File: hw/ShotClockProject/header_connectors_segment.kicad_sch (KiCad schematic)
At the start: 4 parts, among them J1 Conn_01x06_Pin

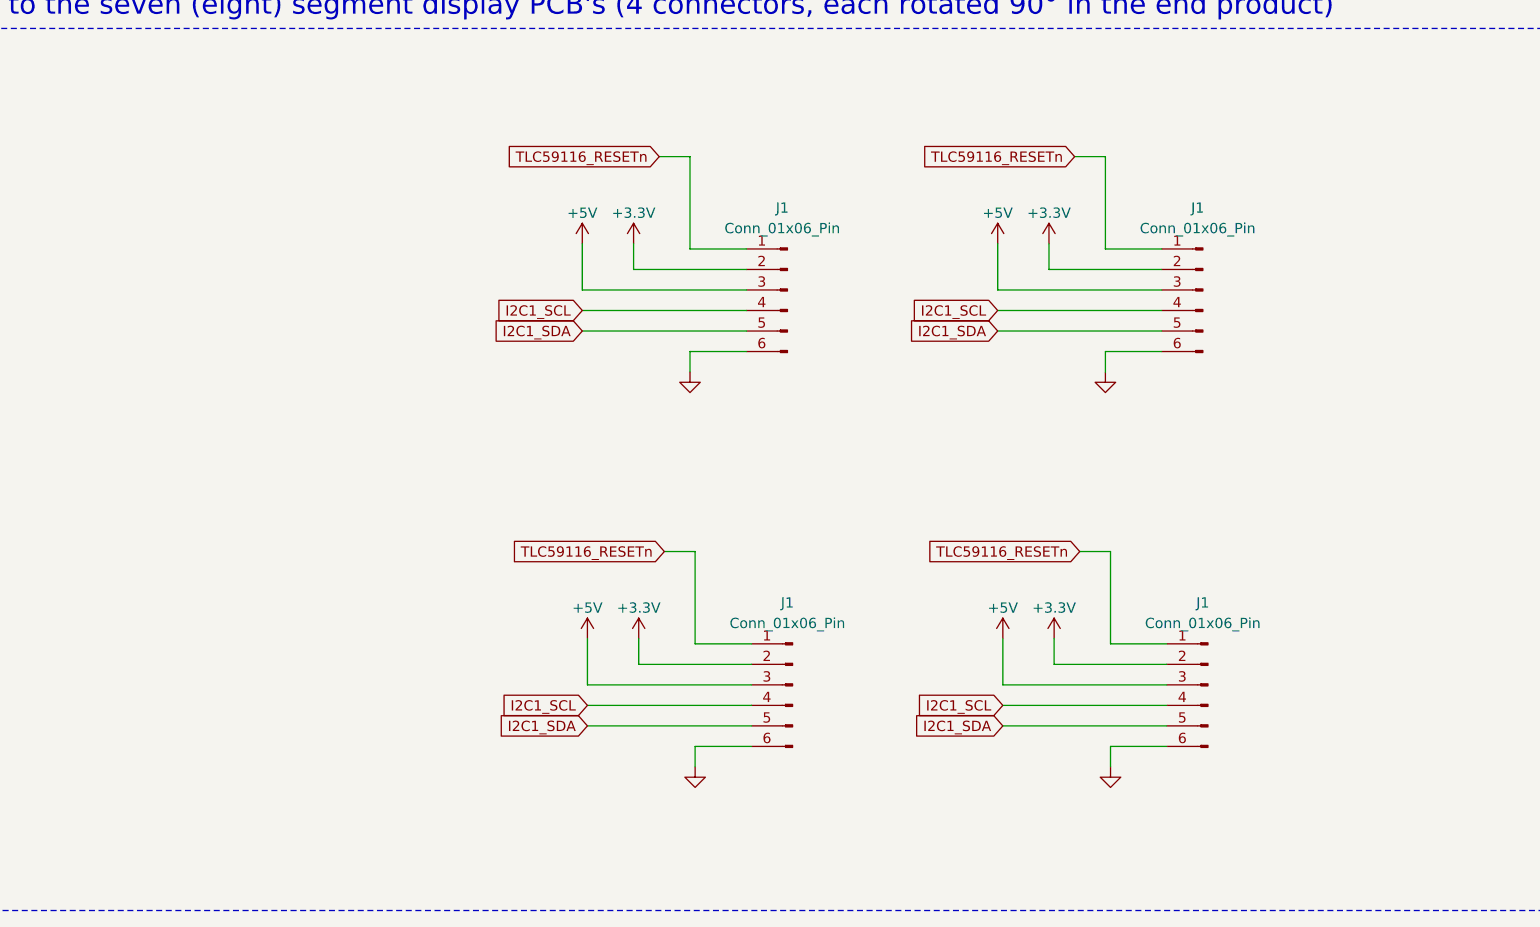
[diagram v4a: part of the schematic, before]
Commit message: Changed display connectors to JST PH 2.0mm
In docs, schematic and footprints
Both sides, connect with male/male cable
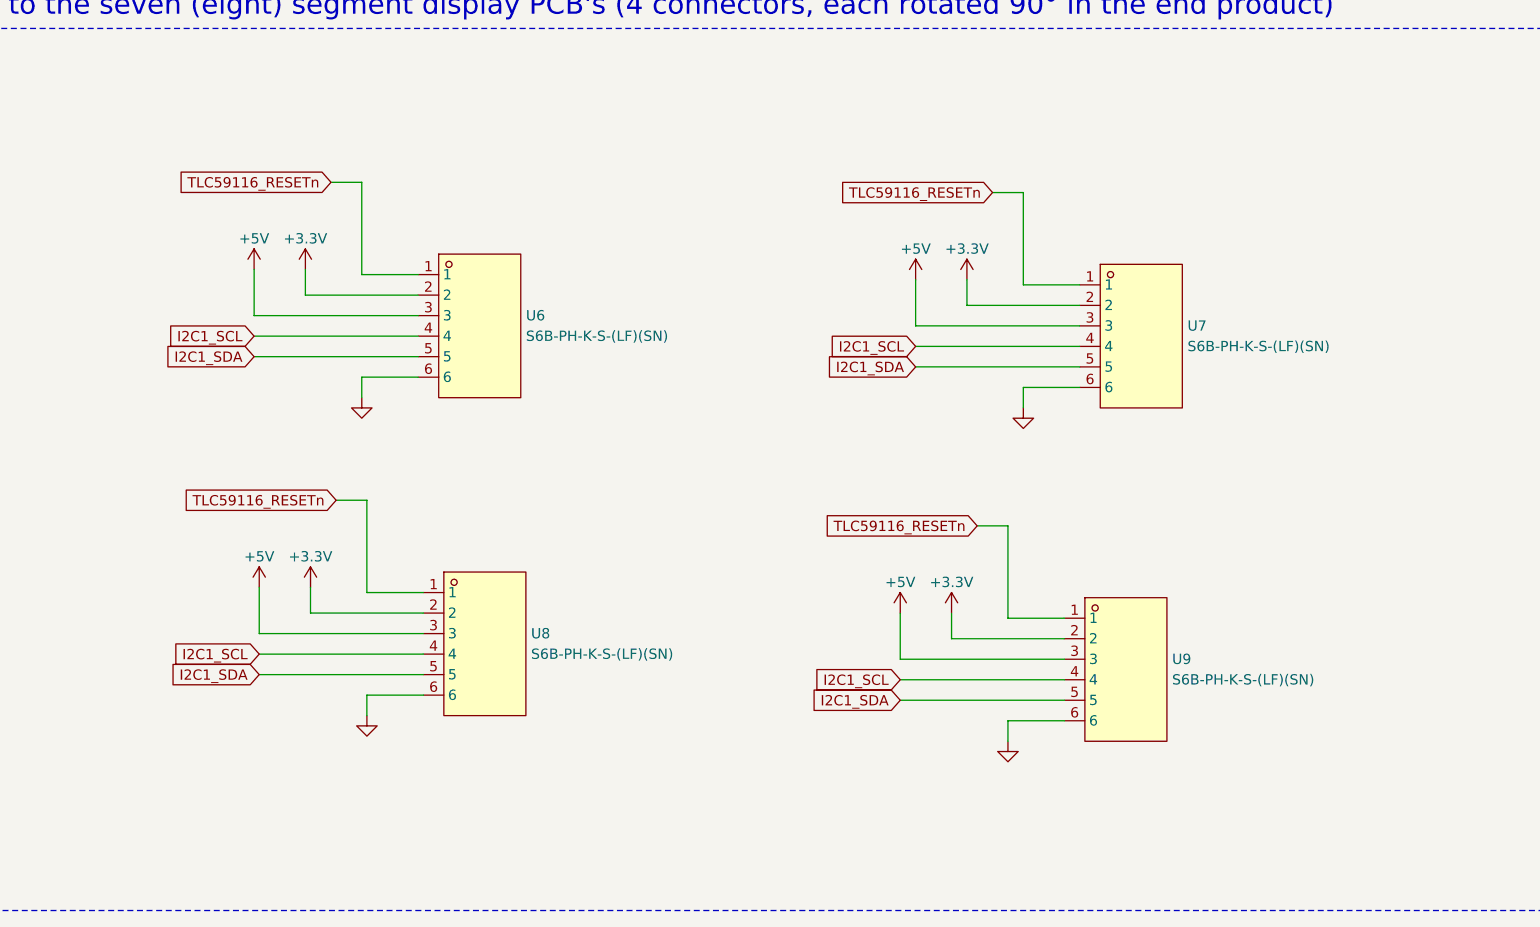
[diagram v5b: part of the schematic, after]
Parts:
- removed J1 (x4): Conn_01x06_Pin, Connector_PinSocket_2.54mm:PinSocket_1x06_P2.54mm_Horizontal, symbol Connector:Conn_01x06_Pin
- added U6, U7, U8, U9: S6B-PH-K-S-(LF)(SN), S6B_PH_K_S_LF_SN:CONN-TH_6P-P2.00_S6B-PH-K-S-LF-SN, symbol S6B_PH_K_S_LF_SN:S6B-PH-K-S-(LF)(SN)
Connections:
- net +3.3V: now also U6.2, U7.2, U8.2, U9.2
- net +5V: now also U6.3, U7.3, U8.3, U9.3
- net GND: now also U6.6, U7.6, U8.6, U9.6
- net I2C1_SCL: now also U6.4, U7.4, U8.4, U9.4
- net I2C1_SDA: now also U6.5, U7.5, U8.5, U9.5
- net TLC59116_RESETn: now also U6.1, U7.1, U8.1, U9.1

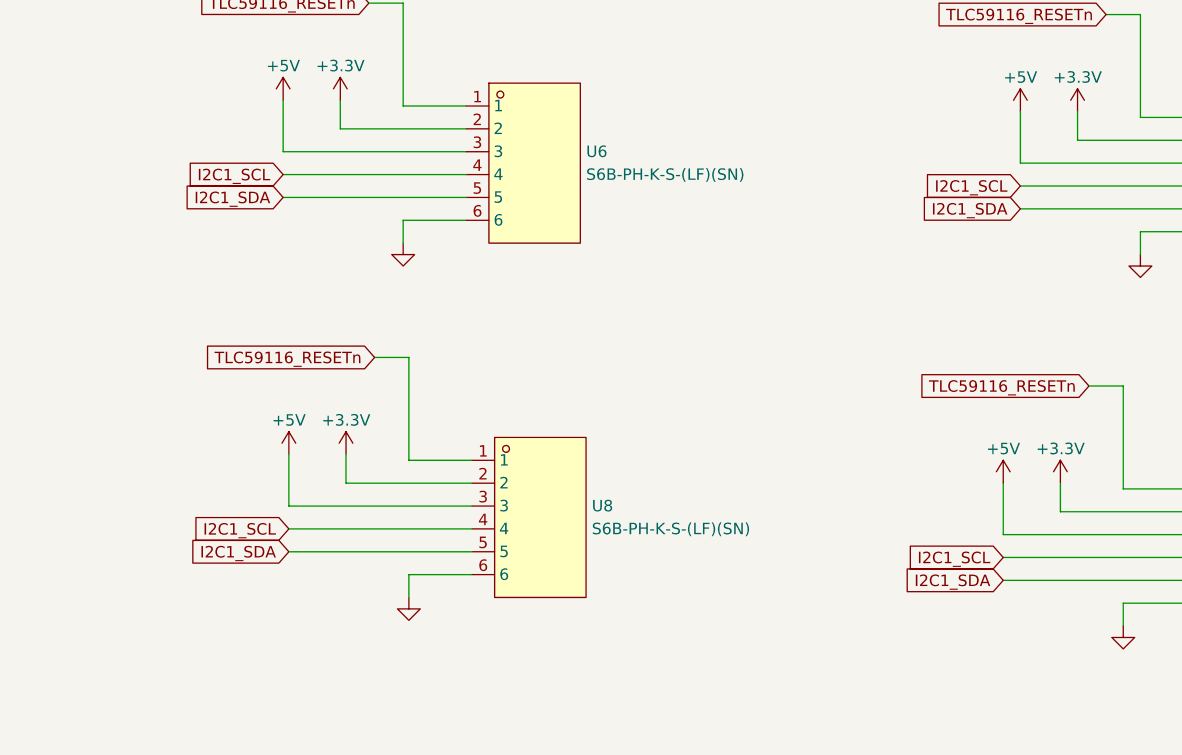
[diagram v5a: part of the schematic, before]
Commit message: Finished mainboard routing
Reconfigered pins to make routing easier/cleaner
Placed copper fills as much as possible to create an even plating index
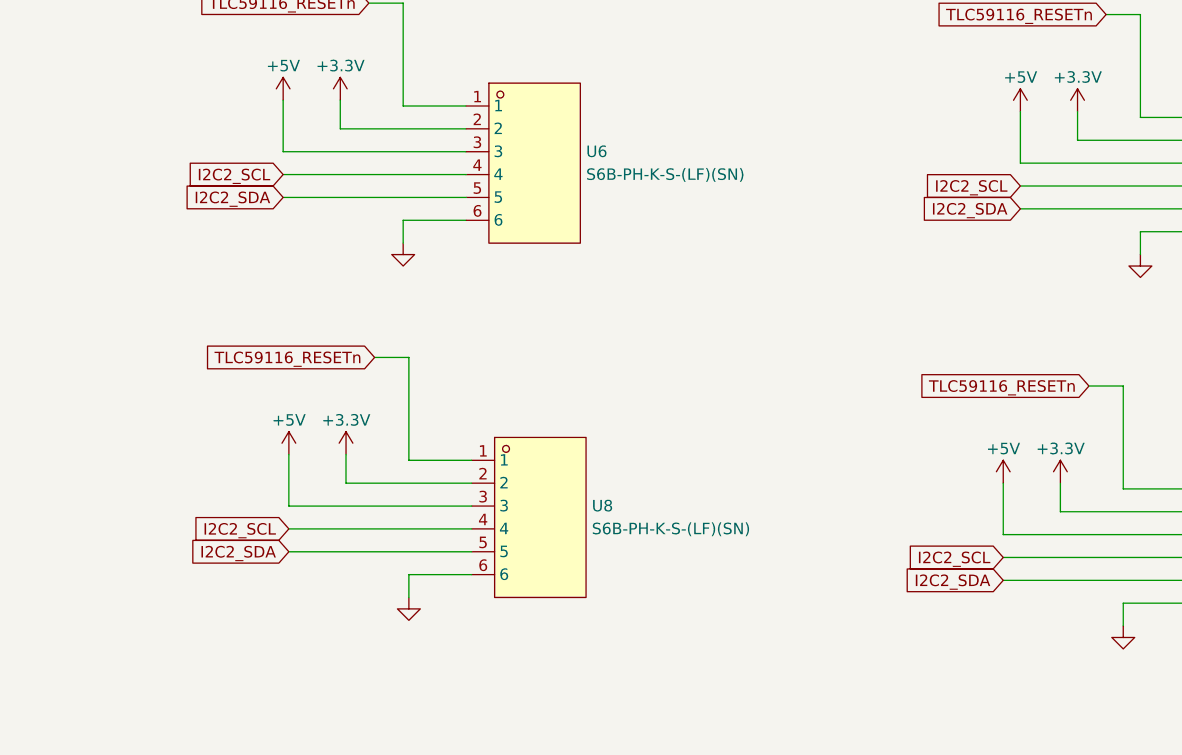
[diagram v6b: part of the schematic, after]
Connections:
- net I2C1_SCL renamed I2C2_SCL
- net I2C1_SDA renamed I2C2_SDA
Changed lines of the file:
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@@
     )
   )
-  (global_label "I2C1_SDA" (shape input) (at 149.225 106.045 180) (fields_autoplaced)
+  (global_label "I2C2_SCL" (shape input) (at 69.85 100.33 180) (fields_autoplaced)
     (effects (font (size 1.27 1.27)) (justify right))
-    (property "Intersheetrefs" "${INTERSHEET_REFS}" (at 137.4103 106.045 0)
-      (effects (font (size 1.27 1.27)) (justify right))
-    )
-  )
-  (global_label "I2C1_SCL" (shape input) (at 149.225 103.505 180) (fields_autoplaced)
-    (effects (font (size 1.27 1.27)) (justify right))
-    (property "Intersheetrefs" "${INTERSHEET_REFS}" (at 137.4708 103.505 0)
-      (effects (font (size 1.27 1.27)) (justify right))
-    )
-  )
-  (global_label "I2C1_SCL" (shape input) (at 151.13 62.23 180) (fields_autoplaced)
-    (effects (font (size 1.27 1.27)) (justify right))
-    (property "Intersheetrefs" "${INTERSHEET_REFS}" (at 139.3758 62.23 0)
-      (effects (font (size 1.27 1.27)) (justify right))
-    )
-  )
-  (global_label "I2C1_SDA" (shape input) (at 69.85 102.87 180) (fields_autoplaced)
-    (effects (font (size 1.27 1.27)) (justify right))
-    (property "Intersheetrefs" "${INTERSHEET_REFS}" (at 58.0353 102.87 0)
+    (property "Intersheetrefs" "${INTERSHEET_REFS}" (at 58.0958 100.33 0)
       (effects (font (size 1.27 1.27)) (justify right))
     )
@@
     )
   )
-  (global_label "I2C1_SDA" (shape input) (at 69.215 63.5 180) (fields_autoplaced)
+  (global_label "I2C2_SDA" (shape input) (at 69.85 102.87 180) (fields_autoplaced)
+    (effects (font (size 1.27 1.27)) (justify right))
+    (property "Intersheetrefs" "${INTERSHEET_REFS}" (at 58.0353 102.87 0)
+      (effects (font (size 1.27 1.27)) (justify right))
+    )
+  )
+  (global_label "I2C2_SDA" (shape input) (at 69.215 63.5 180) (fields_autoplaced)
     (effects (font (size 1.27 1.27)) (justify right))
     (property "Intersheetrefs" "${INTERSHEET_REFS}" (at 57.4003 63.5 0)
+      (effects (font (size 1.27 1.27)) (justify right))
+    )
+  )
+  (global_label "I2C2_SDA" (shape input) (at 149.225 106.045 180) (fields_autoplaced)
+    (effects (font (size 1.27 1.27)) (justify right))
+    (property "Intersheetrefs" "${INTERSHEET_REFS}" (at 137.4103 106.045 0)
       (effects (font (size 1.27 1.27)) (justify right))
     )
@@
     )
   )
-  (global_label "I2C1_SDA" (shape input) (at 151.13 64.77 180) (fields_autoplaced)
+  (global_label "I2C2_SCL" (shape input) (at 151.13 62.23 180) (fields_autoplaced)
     (effects (font (size 1.27 1.27)) (justify right))
-    (property "Intersheetrefs" "${INTERSHEET_REFS}" (at 139.3153 64.77 0)
+    (property "Intersheetrefs" "${INTERSHEET_REFS}" (at 139.3758 62.23 0)
       (effects (font (size 1.27 1.27)) (justify right))
     )
@@
     )
   )
-  (global_label "I2C1_SCL" (shape input) (at 69.215 60.96 180) (fields_autoplaced)
+  (global_label "I2C2_SCL" (shape input) (at 149.225 103.505 180) (fields_autoplaced)
+    (effects (font (size 1.27 1.27)) (justify right))
+    (property "Intersheetrefs" "${INTERSHEET_REFS}" (at 137.4708 103.505 0)
+      (effects (font (size 1.27 1.27)) (justify right))
+    )
+  )
+  (global_label "I2C2_SCL" (shape input) (at 69.215 60.96 180) (fields_autoplaced)
     (effects (font (size 1.27 1.27)) (justify right))
     (property "Intersheetrefs" "${INTERSHEET_REFS}" (at 57.4608 60.96 0)
@@
     )
   )
-  (global_label "I2C1_SCL" (shape input) (at 69.85 100.33 180) (fields_autoplaced)
+  (global_label "I2C2_SDA" (shape input) (at 151.13 64.77 180) (fields_autoplaced)
     (effects (font (size 1.27 1.27)) (justify right))
-    (property "Intersheetrefs" "${INTERSHEET_REFS}" (at 58.0958 100.33 0)
+    (property "Intersheetrefs" "${INTERSHEET_REFS}" (at 139.3153 64.77 0)
       (effects (font (size 1.27 1.27)) (justify right))
     )
